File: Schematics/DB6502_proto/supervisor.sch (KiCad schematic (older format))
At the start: 33 parts, among them J4 AVR ISP, J5 Debug UART, J6 USB_B, U14 74AC74, U15 ATmega644PA-PU, U16 74HC74, U17 74HC595, U18 74HC157, U19 FT230XS, U7 74AC04, U9 74AC08, Y1 20MHz

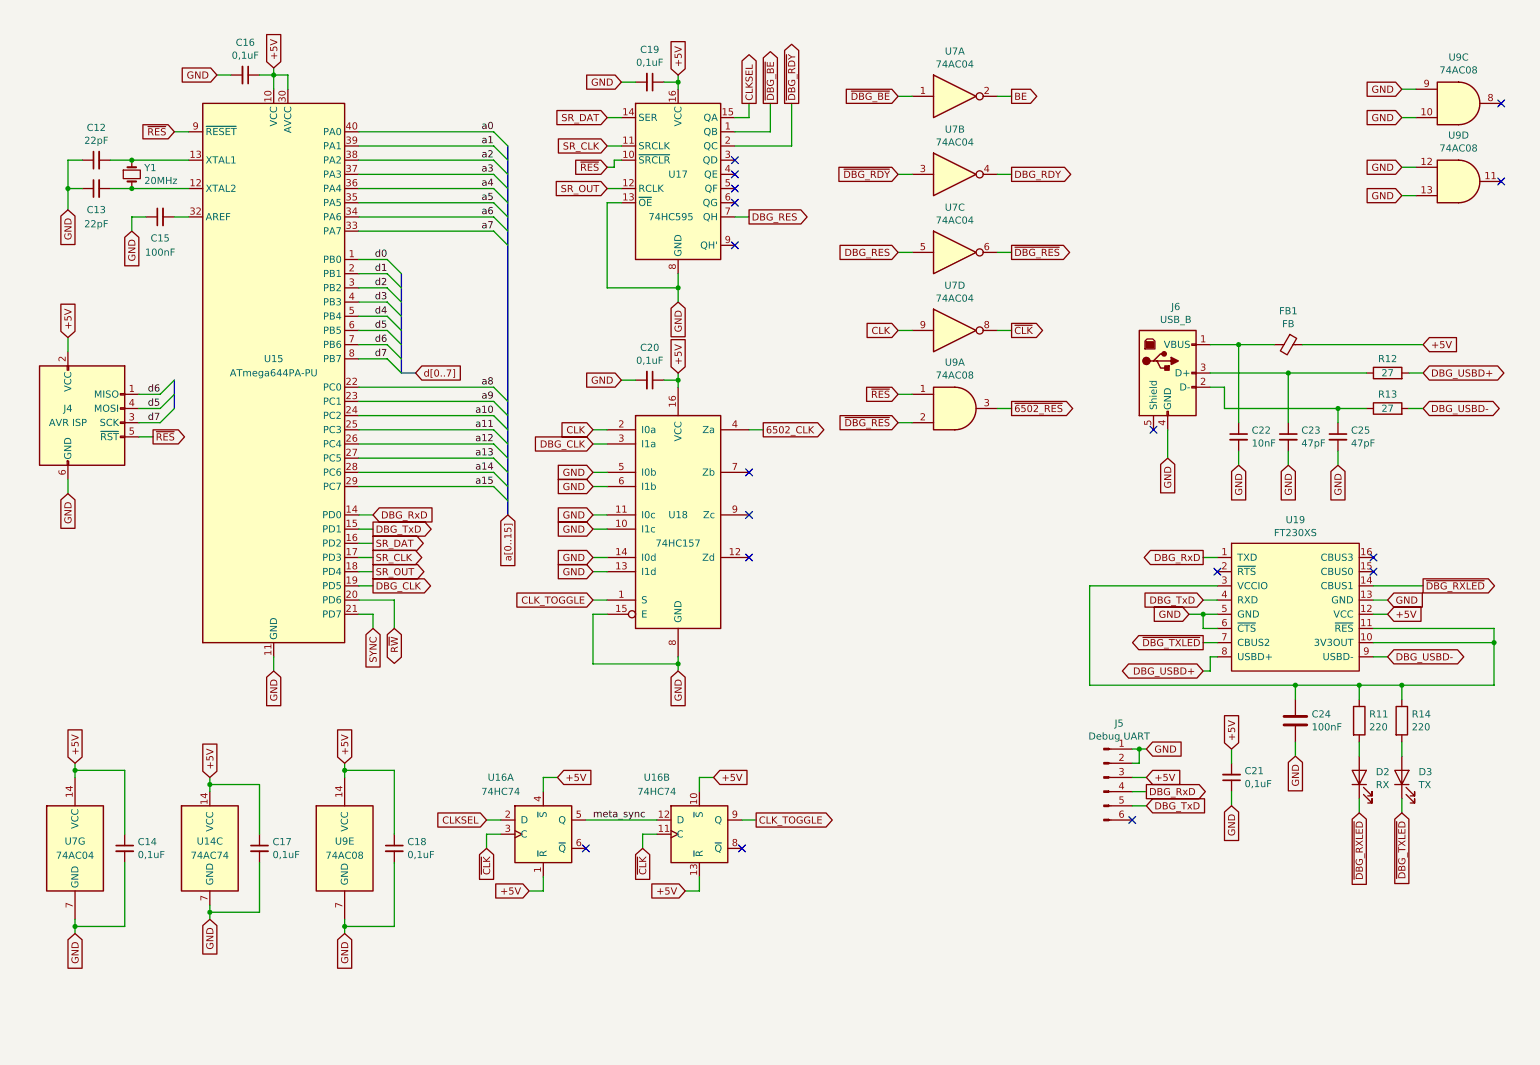
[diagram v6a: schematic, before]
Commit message: Added second USB channel to UART
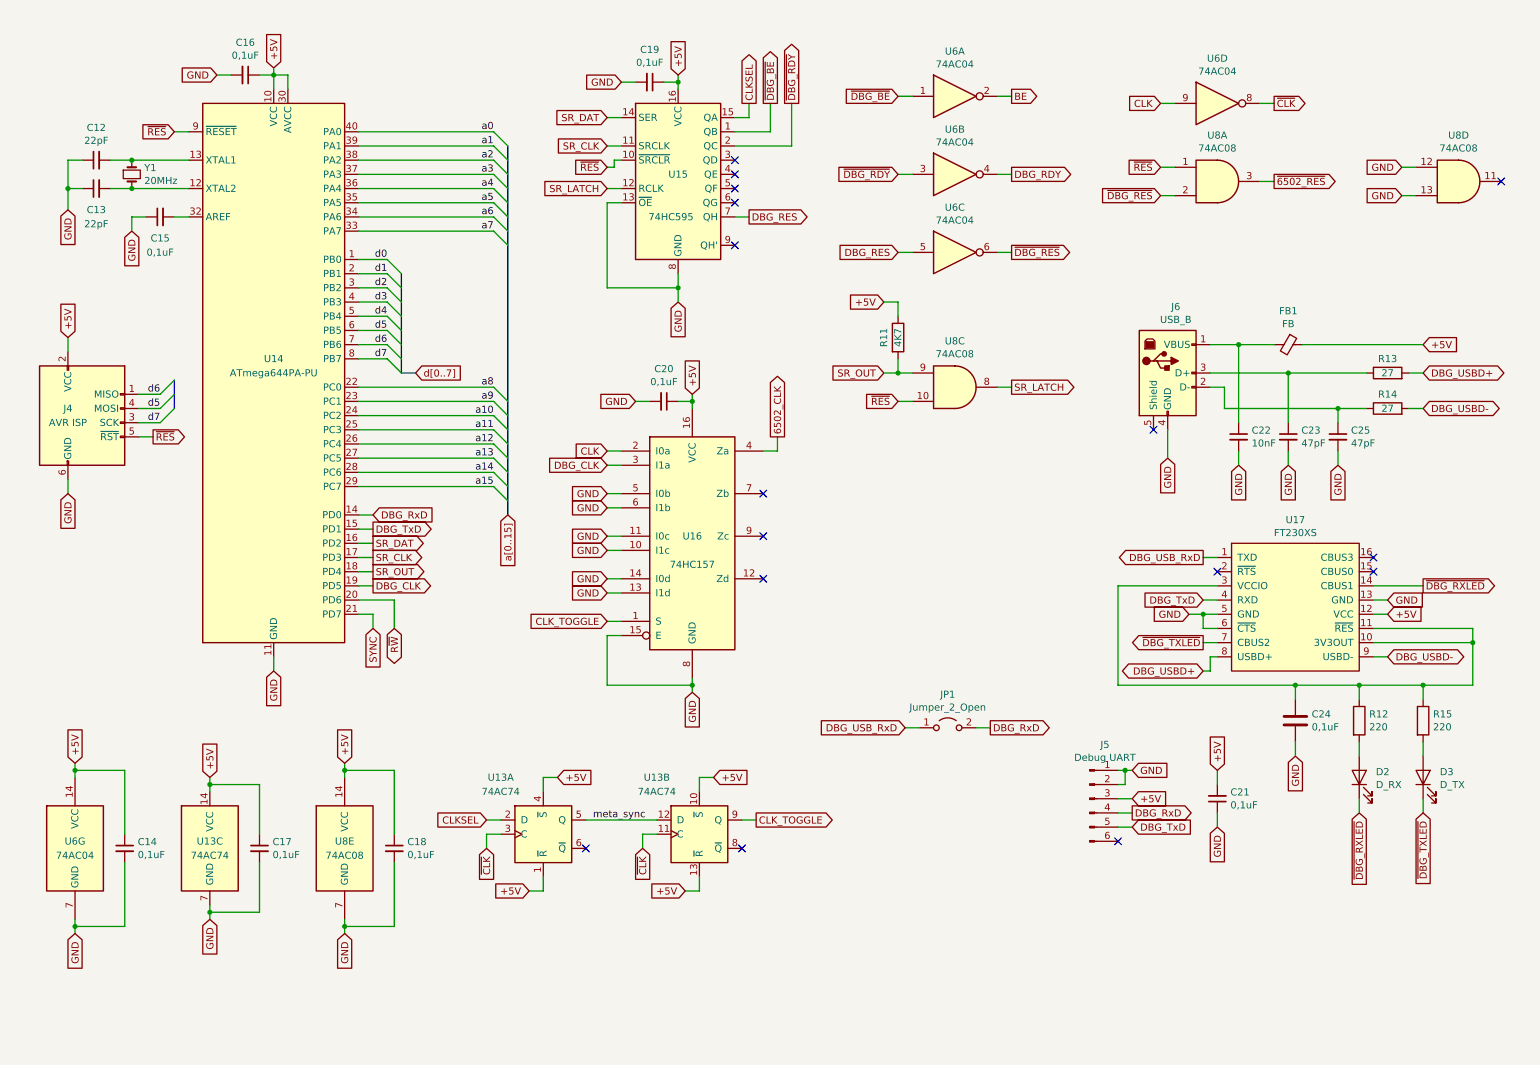
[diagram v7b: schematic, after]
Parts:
- added JP1: Jumper_2_Open, Connector_PinHeader_2.54mm:PinHeader_2x01_P2.54mm_Vertical, symbol Jumper:Jumper_2_Open
- added R11: 4K7, Resistor_THT:R_Axial_DIN0207_L6.3mm_D2.5mm_P10.16mm_Horizontal, symbol Device:R
- C14, C16, C17, C18, C19, C20, C21: footprint (none) -> Capacitor_THT:C_Disc_D5.0mm_W2.5mm_P2.50mm
- C15, C24: value 100nF -> 0,1uF
- D2: value RX -> D_RX
- D3: value TX -> D_TX
- U13: renamed from U14; footprint (none) -> Package_DIP:DIP-14_W7.62mm_Socket
- U13: renamed from U16; value 74HC74 -> 74AC74; footprint (none) -> Package_DIP:DIP-14_W7.62mm_Socket
- U15: renamed from U17; footprint (none) -> Package_DIP:DIP-16_W7.62mm_Socket
- U16: renamed from U18; footprint (none) -> Package_DIP:DIP-16_W7.62mm_Socket
- U6: renamed from U7; footprint (none) -> Package_DIP:DIP-14_W7.62mm_Socket
- U8: renamed from U9; footprint (none) -> Package_DIP:DIP-14_W7.62mm_Socket
- renumbered R11 to R12, R12 to R13, R13 to R14, R14 to R15, U15 to U14, U19 to U17
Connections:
- net +5V: now also R11.1
- net DBG_RxD: now also JP1.2 (B); no longer U17.1 (TXD)
- net GND: no longer U8.10, U8.9
- net SR_OUT: now also U8.9, R11.2; no longer U15.12 (RCLK)
- net ~RES: now also U8.10
- net SR_LATCH: now reaches U8.8
- net SR_LATCH: now also U15.12 (RCLK)
- new net DBG_USB_RxD: JP1.1 (A), U17.1 (TXD)
- no-connect marks 17 -> 16
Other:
- moved on the sheet: C20, C21, D3, J5, R15, U16, U6D, U8A, U8C

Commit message: Updated schematic to reflect PLD WS generator
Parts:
- removed C22: 10nF, Capacitor_THT:C_Disc_D5.0mm_W2.5mm_P2.50mm, symbol Device:C_Small
- removed C23: 47pF, Capacitor_THT:C_Disc_D5.0mm_W2.5mm_P2.50mm, symbol Device:C_Small
- removed FB1: FB, Resistor_THT:R_Axial_DIN0207_L6.3mm_D2.5mm_P10.16mm_Horizontal, symbol Device:Ferrite_Bead_Small
- removed J5: Debug UART, Connector_PinHeader_2.54mm:PinHeader_1x06_P2.54mm_Horizontal, symbol Connector:Conn_01x06_Male
- removed J6: USB_B, Connector_USB:USB_B_OST_USB-B1HSxx_Horizontal, symbol 6502:USB_B
- removed JP1: Jumper_2_Open, Connector_PinHeader_2.54mm:PinHeader_2x01_P2.54mm_Vertical, symbol Jumper:Jumper_2_Open
- removed R12, R15: 220, Resistor_THT:R_Axial_DIN0207_L6.3mm_D2.5mm_P10.16mm_Horizontal, symbol Device:R
- removed R13, R14: 27, Resistor_THT:R_Axial_DIN0207_L6.3mm_D2.5mm_P10.16mm_Horizontal, symbol Device:R
- added R18, R19: 220, Resistor_THT:R_Axial_DIN0207_L6.3mm_D2.5mm_P10.16mm_Horizontal, symbol Device:R
- added SW1: Reset, Button_Switch_THT:SW_PUSH_6mm_H4.3mm, symbol Switch:SW_Push
- added U7: DS1813, Package_TO_SOT_THT:TO-92_Inline_Wide, symbol 6502:DS1813
- added unit 5 of U8
- added X1: 14MHz, Oscillator:Oscillator_DIP-14, symbol Oscillator:ACO-xxxMHz
- C24: symbol Device:C -> Device:C_Small
- C25: value 47pF -> 0,1uF
- D2: value D_RX -> D_TX
- D3: value D_TX -> D_RX
- renumbered C12 to C16, C13 to C17, C14 to C18, C15 to C19, C16 to C20, C17 to C21, C18 to C22, C19 to C23, C20 to C26, C21 to C27, J4 to J10, R11 to R17, U14 to U10, U15 to U11, U17 to U12, U16 to U13, U8 to U6, U6 to U8, U13 to U9
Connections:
- net +5V: now also C25.1, C27.1, U7.2 (VCC), X1.14 (Vcc); no longer C27.2
- net CLK: now also X1.8 (OUT)
- net GND: now also C27.2, SW1.2, U7.3 (GND), U8.11, X1.7 (GND); no longer C27.1
- net ~DBG_RXLED: now also D3.1 (K); no longer D2.1 (K)
- net ~DBG_TXLED: now also D2.1 (K); no longer D3.1 (K)
- net ~RES: now also SW1.1, U7.1 (~RST)
- net at C24.1, U12.10 (3V3OUT), U12.11 (~RES)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: now also R18.1, R19.1
- net at D2.2 (A): now also R18.2
- net at D3.2 (A): now also R19.2
- no-connect marks 16 -> 15
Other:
- moved on the sheet: C18, C21, C22, C24, C26, C27, J10, R17, U12, U13, U6A, U6C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
